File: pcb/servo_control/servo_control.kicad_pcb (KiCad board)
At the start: 2 copper layers, 94.6 x 66.7 mm, 75 parts, among them J1 Jack-DC, J10 Conn_01x03_Female, J11 Conn_01x03_Female, J12 Conn_01x03_Female, J13 Conn_01x03_Female, J14 Conn_01x03_Female, J15 Conn_01x03_Female, J16 Conn_01x03_Female, J17 Conn_01x03_Female, J18 Conn_01x03_Female, J19 Conn_01x03_Female, J2 YLIDAR X4, J20 Conn_01x03_Female, J21 Conn_01x06_Male, J22 GY-87, J3 Conn_01x03_Female, J4 Conn_01x03_Female, J5 Conn_01x03_Female, J6 Conn_01x03_Female, J7 Conn_01x03_Female, J8 Conn_01x03_Female, J9 Conn_01x03_Female, SW1 ESP_PROG, SW2 ESP_RST, U1 ATmega2560-16A, U2 LM317-3.3_SOT-223, U3 ESP32-WROOM-32, U4 MCP73213-A6SI/MF, U6 LM317-5_SOT-223, U7 LT1085-ADJ

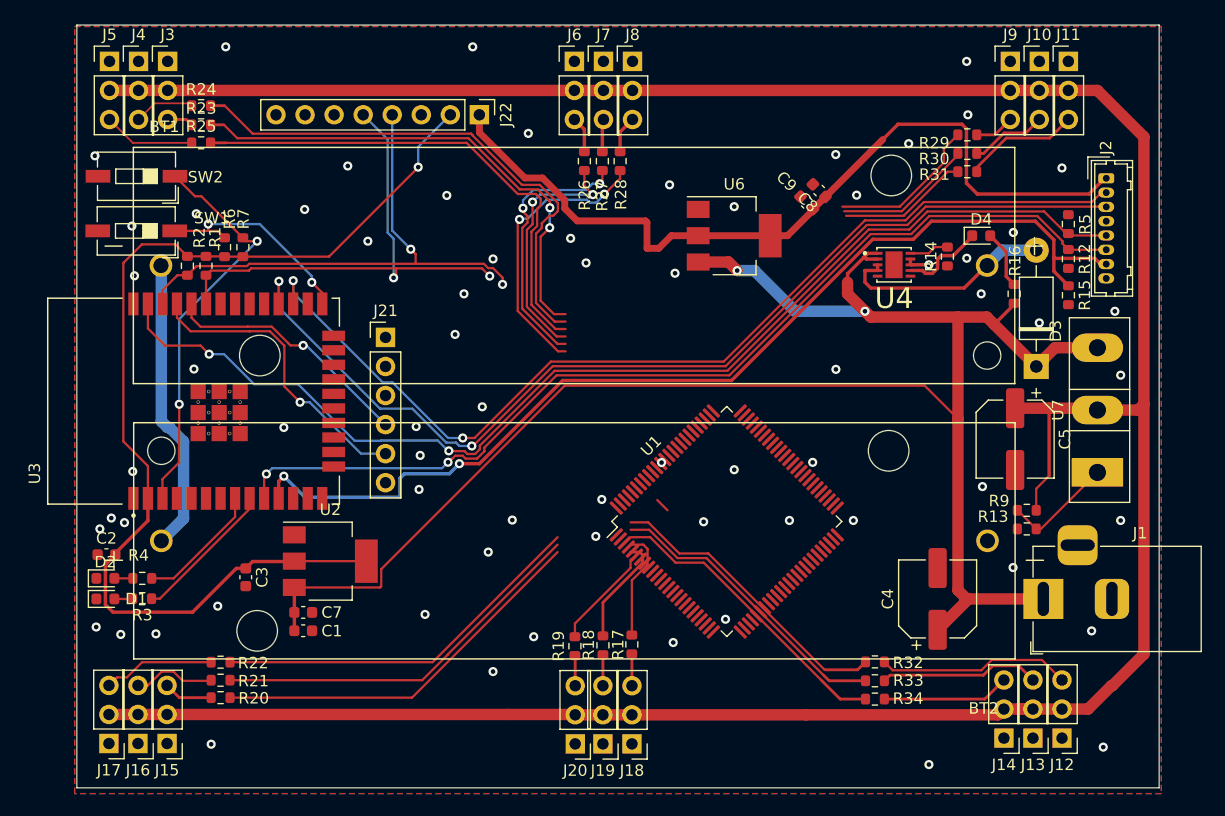
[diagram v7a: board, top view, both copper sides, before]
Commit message: add atmega2560 servos wiring
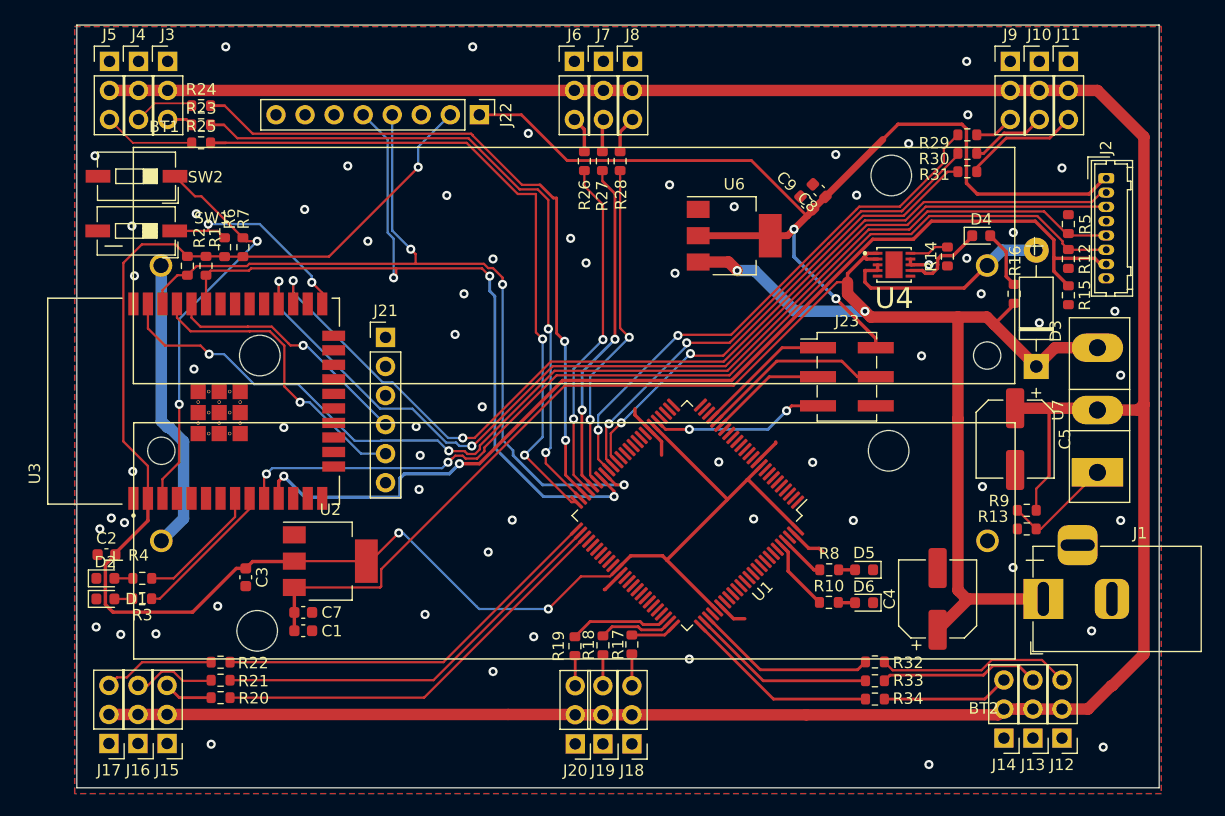
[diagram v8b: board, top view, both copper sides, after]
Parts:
- added D5: LED, LED_SMD:LED_0603_1608Metric, F.Cu at (170.1, 87.6)
- added D6: LED, LED_SMD:LED_0603_1608Metric, F.Cu at (170.1, 90.5)
- added J23: AVR-ISP-6, Connector_PinHeader_2.54mm:PinHeader_2x03_P2.54mm_Vertical_SMD, F.Cu at (168.6, 70.8)
- added R10: 1K, Resistor_SMD:R_0603_1608Metric, F.Cu at (167.0, 90.5)
- added R8: 1K, Resistor_SMD:R_0603_1608Metric, F.Cu at (167.1, 87.6)
- moved U1 3.51 mm to (154.6, 82.9), turned to -135 degrees
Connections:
- U1 pad 10: Net-(U1-VCC-Pad10) -> 3.3V
- U1 pad 100: unconnected-(U1-AVCC-Pad100) -> 3.3V
- U1 pad 11: Net-(U1-GND-Pad11) -> GND
- U1 pad 20: unconnected-(U1-PB1-Pad20) -> SCK
- U1 pad 21: unconnected-(U1-PB2-Pad21) -> MOSI
- U1 pad 22: unconnected-(U1-PB3-Pad22) -> MISO
- U1 pad 30: unconnected-(U1-~{RESET}-Pad30) -> RST
- U1 pad 31: Net-(U1-VCC-Pad10) -> 3.3V
- U1 pad 32: Net-(U1-GND-Pad11) -> GND
- U1 pad 40: unconnected-(U1-PL5-Pad40) -> PWM_0_8
- U1 pad 41: unconnected-(U1-PL6-Pad41) -> PWM_0_7
- U1 pad 42: unconnected-(U1-PL7-Pad42) -> PWM_0_6
- U1 pad 43: unconnected-(U1-PD0-Pad43) -> I2C_SCL
- U1 pad 44: unconnected-(U1-PD1-Pad44) -> I2C_SDA
- U1 pad 45: unconnected-(U1-PD2-Pad45) -> PWM_0_5
- U1 pad 46: unconnected-(U1-PD3-Pad46) -> PWM_0_4
- U1 pad 47: unconnected-(U1-PD4-Pad47) -> PWM_0_3
- U1 pad 48: unconnected-(U1-PD5-Pad48) -> PWM_0_1
- U1 pad 49: unconnected-(U1-PD6-Pad49) -> PWM_0_0
- U1 pad 50: unconnected-(U1-PD7-Pad50) -> PWM_0_2
- U1 pad 51: unconnected-(U1-PG0-Pad51) -> PWM_1_5
- U1 pad 52: unconnected-(U1-PG1-Pad52) -> PWM_1_6
- U1 pad 53: unconnected-(U1-PC0-Pad53) -> PWM_1_7
- U1 pad 61: Net-(U1-VCC-Pad10) -> 3.3V
- U1 pad 62: Net-(U1-GND-Pad11) -> GND
- U1 pad 73: unconnected-(U1-PA5-Pad73) -> PWM_1_8
- U1 pad 74: unconnected-(U1-PA4-Pad74) -> PWM_1_9
- U1 pad 75: unconnected-(U1-PA3-Pad75) -> PWM_1_10
- U1 pad 76: unconnected-(U1-PA2-Pad76) -> PWM_1_11
- U1 pad 77: unconnected-(U1-PA1-Pad77) -> PWM_1_12
- U1 pad 78: unconnected-(U1-PA0-Pad78) -> PWM_1_13
- U1 pad 80: Net-(U1-VCC-Pad10) -> 3.3V
- U1 pad 81: Net-(U1-GND-Pad11) -> GND
- U1 pad 96: unconnected-(U1-PF1-Pad96) -> LED_4
- U1 pad 97: unconnected-(U1-PF0-Pad97) -> LED_3
- U1 pad 99: Net-(U1-GND-Pad11) -> GND
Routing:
- net 3.3V: track 93.3 -> 158.7 mm, vias 1 -> 3
- net PWM_0_6: track 13.4 -> 47.5 mm, vias 0 -> 2
- net PWM_0_7: track 12.1 -> 44.6 mm, vias 0 -> 2
- net PWM_0_8: track 11.4 -> 42.7 mm, vias 0 -> 2
- net I2C_SDA: track 44.1 -> 73.7 mm, vias 2 -> 3
- net I2C_SCL: track 46.8 -> 75.0 mm, vias 2 -> 3
- net 5V: track 72.7 -> 91.3 mm, vias 0 -> 2
- net MOSI: track 0.00 -> 16.7 mm
- net PWM_0_2: track 44.3 -> 60.3 mm, vias 0 -> 2
- net PWM_0_0: track 44.1 -> 59.8 mm
- net GND: track 2.38 -> 17.7 mm, vias 69 -> 64
- net RST: track 0.00 -> 15.2 mm, vias 0 -> 2
- net PWM_0_1: track 46.9 -> 60.5 mm, vias 0 -> 2
- net MISO: track 0.00 -> 11.7 mm
- net PWM_1_13: track 26.2 -> 15.9 mm
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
